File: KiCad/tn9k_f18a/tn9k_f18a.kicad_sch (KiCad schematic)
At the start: 9 parts, among them J1 Conn_01x20, J2 Conn_01x20, J3 Conn_01x24, J4 Conn_01x24, J5 Conn_02x04_Counter_Clockwise, J6 Conn_02x08_Odd_Even, U1 SN74LVC245, U2 SN74LVC245, U3 SN74LVC245

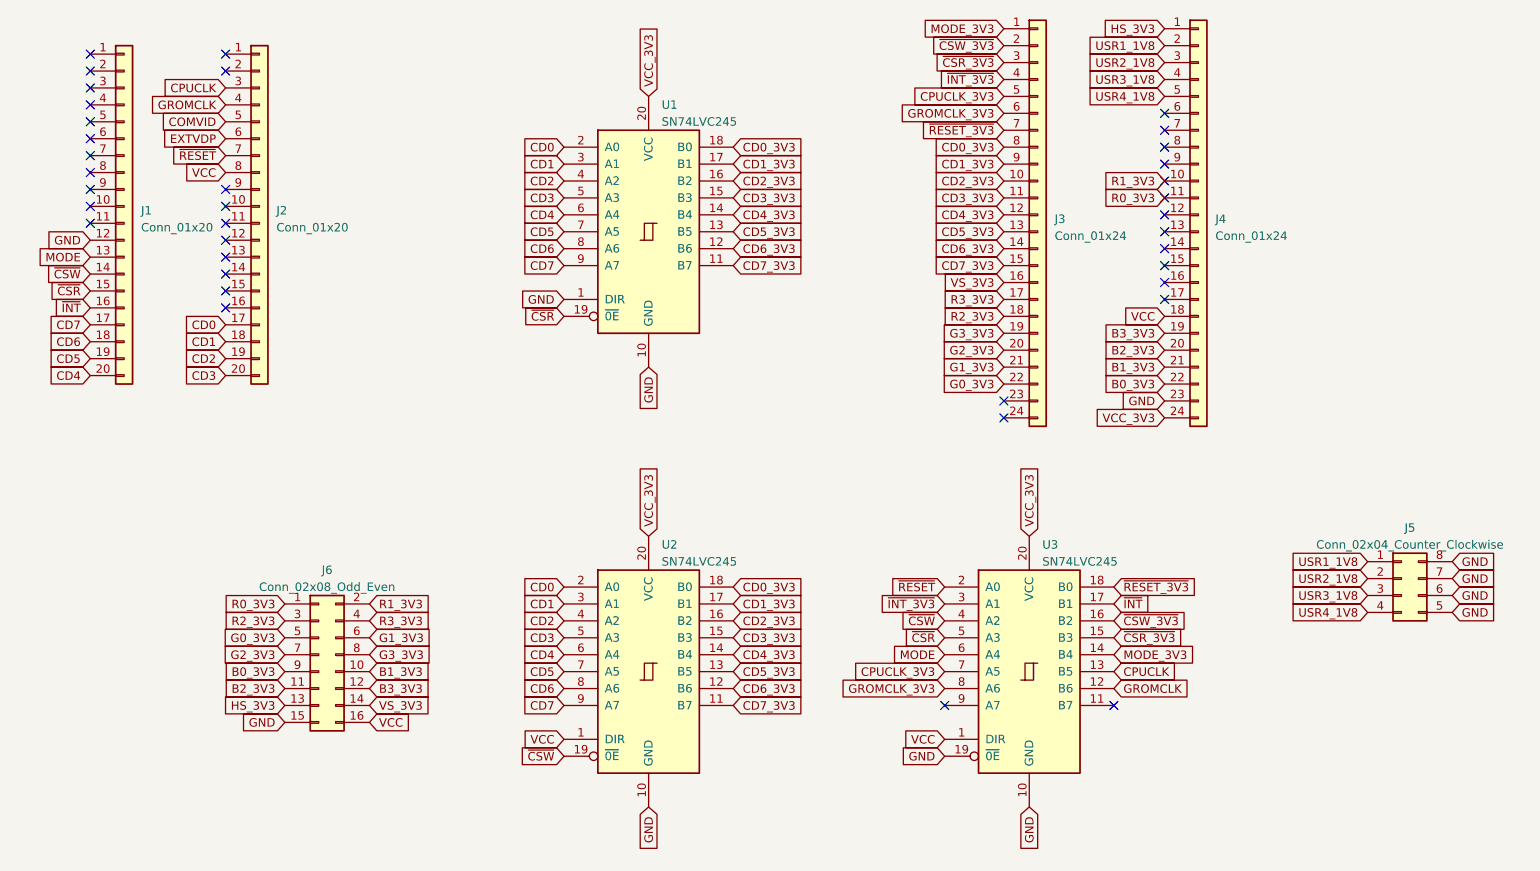
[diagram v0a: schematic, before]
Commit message: update original board adding diode
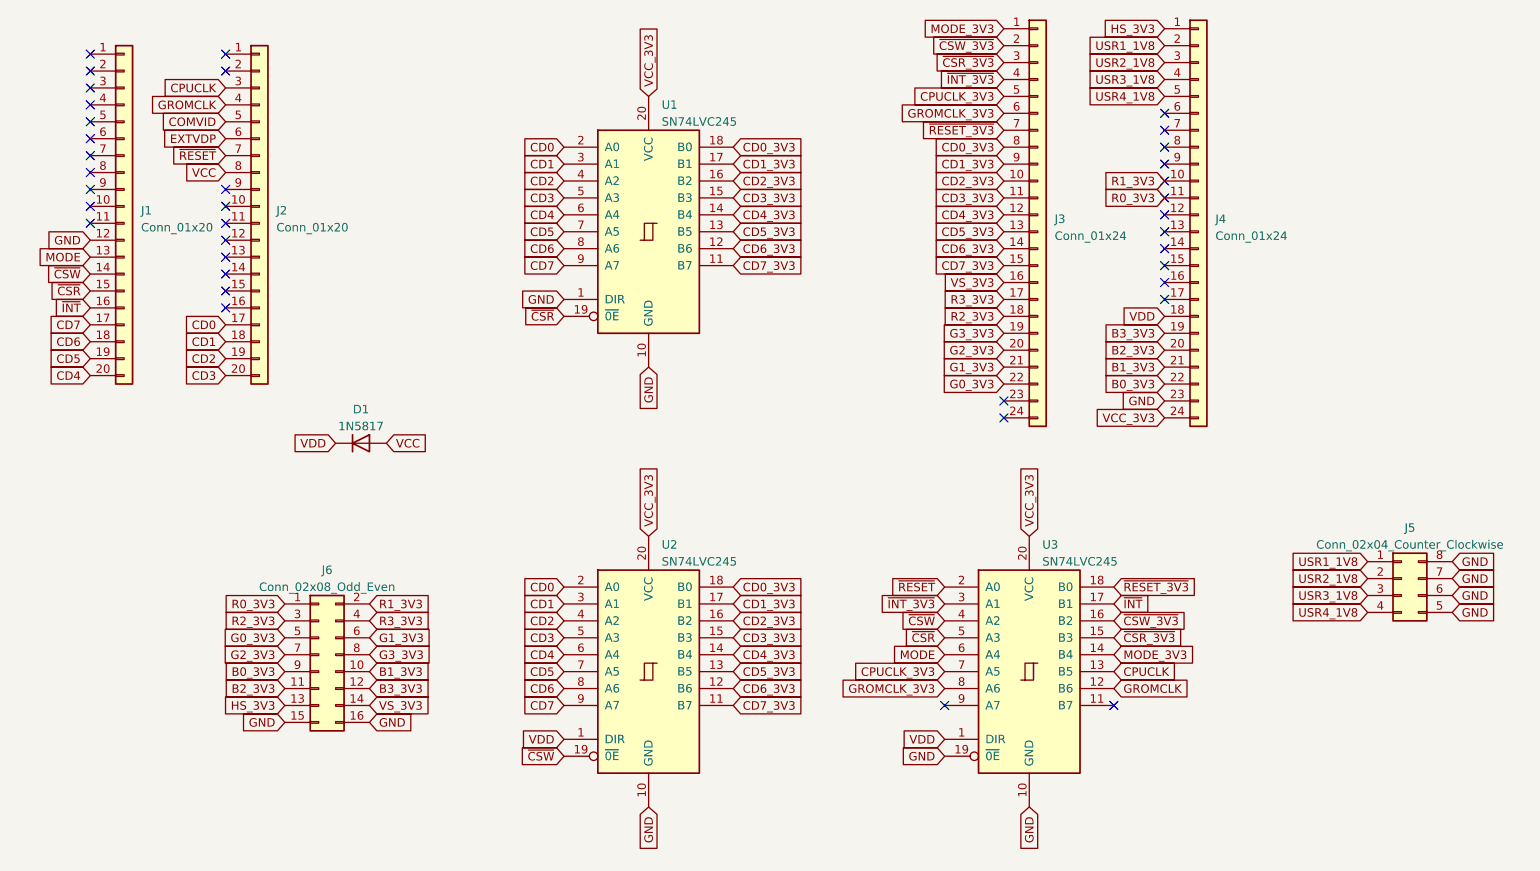
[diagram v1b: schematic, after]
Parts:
- added D1: 1N5817, Diode_THT:D_DO-41_SOD81_P10.16mm_Horizontal, symbol Diode:1N4001
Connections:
- net GND: now also J6.16 (Pin_16)
- net VCC: now also D1.2 (A); no longer J4.18 (Pin_18), J6.16 (Pin_16), U2.1 (DIR), U3.1 (DIR)
- new net VDD: D1.1 (K), J4.18 (Pin_18), U2.1 (DIR), U3.1 (DIR)
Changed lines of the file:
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@@
     )
   )
-  (global_label "VCC" (shape input) (at 226.06 63.5 180) (fields_autoplaced)
+  (global_label "VDD" (shape input) (at 226.06 63.5 180) (fields_autoplaced)
     (effects (font (size 1.27 1.27)) (justify right))
     (property "Intersheetrefs" "${INTERSHEET_REFS}" (at 219.5256 63.5 0)
@@
     )
   )
-  (global_label "VCC" (shape input) (at 193.04 127 180) (fields_autoplaced)
+  (global_label "VDD" (shape input) (at 193.04 127 180) (fields_autoplaced)
     (effects (font (size 1.27 1.27)) (justify right))
     (property "Intersheetrefs" "${INTERSHEET_REFS}" (at 186.5056 127 0)
@@
     )
   )
+  (global_label "VCC" (shape input) (at 109.22 82.55 0) (fields_autoplaced)
+    (effects (font (size 1.27 1.27)) (justify left))
+    (property "Intersheetrefs" "${INTERSHEET_REFS}" (at 115.7544 82.55 0)
+      (effects (font (size 1.27 1.27)) (justify left) hide)
+    )
+  )
   (global_label "VCC" (shape input) (at 85.09 41.91 180) (fields_autoplaced)
     (effects (font (size 1.27 1.27)) (justify right))
@@
     )
   )
-  (global_label "VCC" (shape input) (at 135.89 127 180) (fields_autoplaced)
+  (global_label "VDD" (shape input) (at 135.89 127 180) (fields_autoplaced)
     (effects (font (size 1.27 1.27)) (justify right))
     (property "Intersheetrefs" "${INTERSHEET_REFS}" (at 129.3556 127 0)
@@
     )
   )
+  (global_label "VDD" (shape input) (at 101.6 82.55 180) (fields_autoplaced)
+    (effects (font (size 1.27 1.27)) (justify right))
+    (property "Intersheetrefs" "${INTERSHEET_REFS}" (at 95.0656 82.55 0)
+      (effects (font (size 1.27 1.27)) (justify right) hide)
+    )
+  )
   (global_label "USR4_1V8" (shape input) (at 226.06 30.48 180) (fields_autoplaced)
     (effects (font (size 1.27 1.27)) (justify right))
@@
     )
   )
-  (global_label "VCC" (shape input) (at 106.68 124.46 0) (fields_autoplaced)
-    (effects (font (size 1.27 1.27)) (justify left))
-    (property "Intersheetrefs" "${INTERSHEET_REFS}" (at 113.2144 124.46 0)
+  (global_label "GND" (shape input) (at 106.68 124.46 0) (fields_autoplaced)
+    (effects (font (size 1.27 1.27)) (justify left))
+    (property "Intersheetrefs" "${INTERSHEET_REFS}" (at 113.4563 124.46 0)
       (effects (font (size 1.27 1.27)) (justify left) hide)
     )
@@
     (pin "9")
     (instances
-      (project "TN9K_F18A"
+      (project "tn9k_f18a"
         (path "/e3c6ad0b-efa5-4827-958c-c20bf8519fa1"
           (reference "J1") (unit 1)
@@
     (pin "9")
     (instances
-      (project "TN9K_F18A"
+      (project "tn9k_f18a"
         (path "/e3c6ad0b-efa5-4827-958c-c20bf8519fa1"
           (reference "U3") (unit 1)
@@
     (pin "8")
     (instances
-      (project "TN9K_F18A"
+      (project "tn9k_f18a"
         (path "/e3c6ad0b-efa5-4827-958c-c20bf8519fa1"
           (reference "J5") (unit 1)
@@
     (pin "9")
     (instances
-      (project "TN9K_F18A"
+      (project "tn9k_f18a"
         (path "/e3c6ad0b-efa5-4827-958c-c20bf8519fa1"
           (reference "J3") (unit 1)
@@
     (pin "9")
     (instances
-      (project "TN9K_F18A"
+      (project "tn9k_f18a"
         (path "/e3c6ad0b-efa5-4827-958c-c20bf8519fa1"
           (reference "J6") (unit 1)
@@
     (pin "9")
     (instances
-      (project "TN9K_F18A"
+      (project "tn9k_f18a"
         (path "/e3c6ad0b-efa5-4827-958c-c20bf8519fa1"
           (reference "J2") (unit 1)
@@
     (pin "9")
     (instances
-      (project "TN9K_F18A"
+      (project "tn9k_f18a"
         (path "/e3c6ad0b-efa5-4827-958c-c20bf8519fa1"
           (reference "U1") (unit 1)
+        )
+      )
+    )
+  )
+  (symbol (lib_id "Diode:1N4001") (at 105.41 82.55 0) (unit 1)
+    (in_bom yes) (on_board yes) (dnp no) (fields_autoplaced)
+    (property "Reference" "D1" (at 105.41 77.47 0)
+      (effects (font (size 1.27 1.27)))
+    )
+    (property "Value" "1N5817" (at 105.41 80.01 0)
+      (effects (font (size 1.27 1.27)))
+    )
+    (property "Footprint" "Diode_THT:D_DO-41_SOD81_P10.16mm_Horizontal" (at 105.41 82.55 0)
+      (effects (font (size 1.27 1.27)) hide)
+    )
+    (property "Datasheet" "http://www.vishay.com/docs/88503/1n4001.pdf" (at 105.41 82.55 0)
+      (effects (font (size 1.27 1.27)) hide)
+    )
+    (property "Sim.Device" "D" (at 105.41 82.55 0)
+      (effects (font (size 1.27 1.27)) hide)
+    )
+    (property "Sim.Pins" "1=K 2=A" (at 105.41 82.55 0)
+      (effects (font (size 1.27 1.27)) hide)
+    )
+    (pin "1")
+    (pin "2")
+    (instances
+      (project "tn9k_f18a"
+        (path "/e3c6ad0b-efa5-4827-958c-c20bf8519fa1"
+          (reference "D1") (unit 1)
         )
       )
@@
     (pin "9")
     (instances
-      (project "TN9K_F18A"
+      (project "tn9k_f18a"
         (path "/e3c6ad0b-efa5-4827-958c-c20bf8519fa1"
           (reference "J4") (unit 1)
@@
     (pin "9")
     (instances
-      (project "TN9K_F18A"
+      (project "tn9k_f18a"
         (path "/e3c6ad0b-efa5-4827-958c-c20bf8519fa1"
           (reference "U2") (unit 1)
